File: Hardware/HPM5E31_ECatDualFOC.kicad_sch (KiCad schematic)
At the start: 19 parts, among them J15 HR911205C, U34 M3, U38 M3, U46 M3, U47 M3

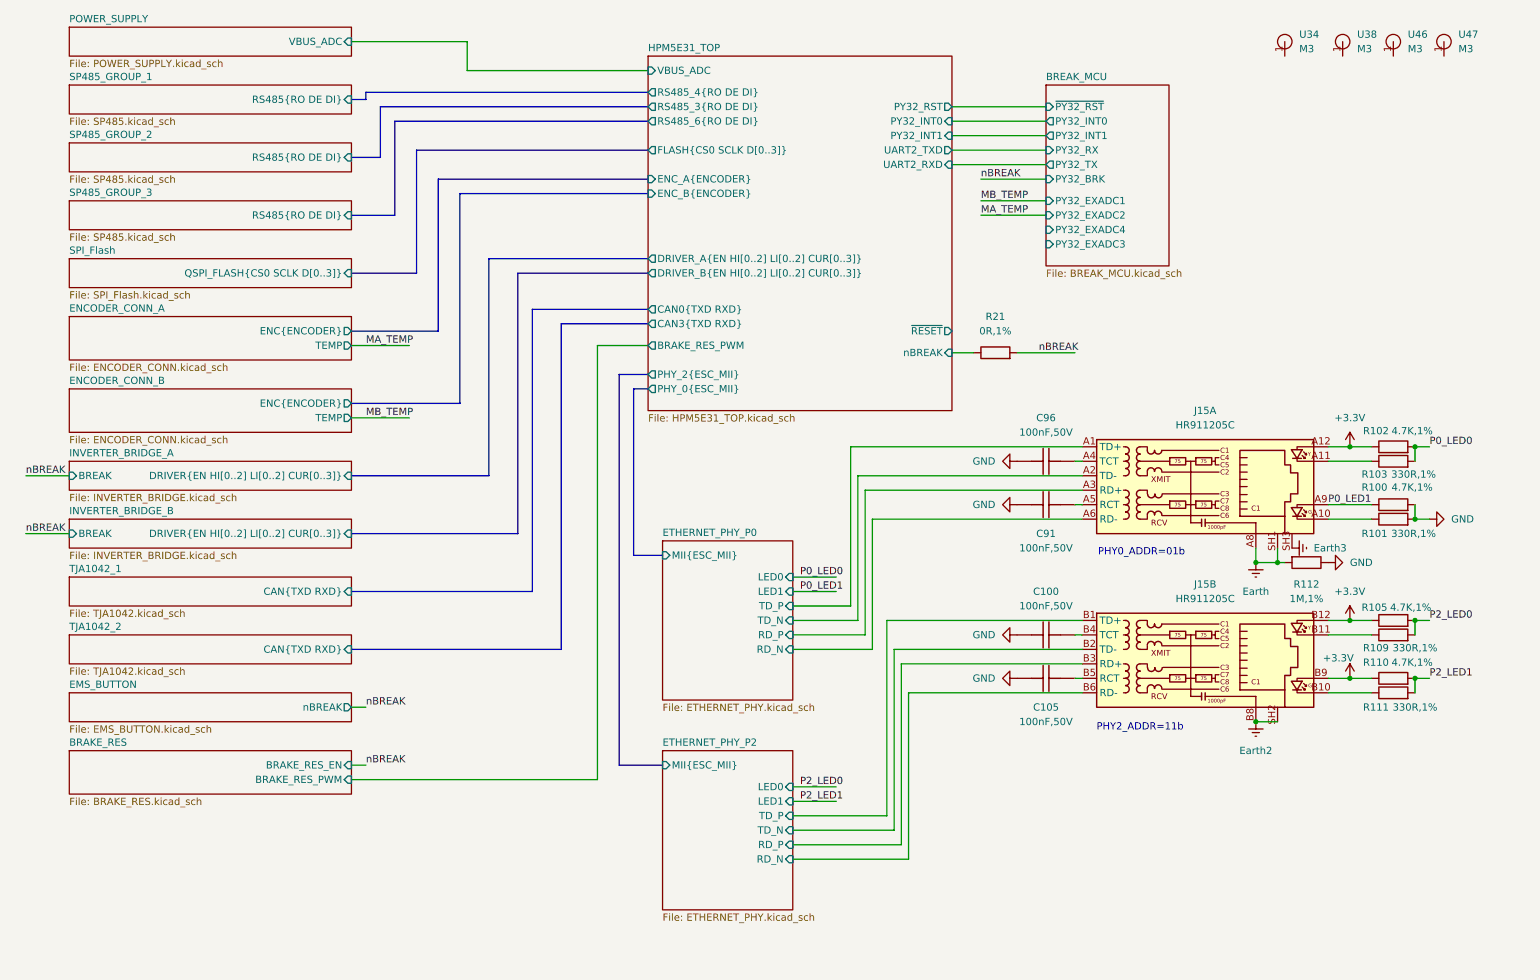
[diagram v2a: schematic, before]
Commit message: PCB：风扇增加控制IO，泄放驱动增加使能引脚，485编码器电源接入控制
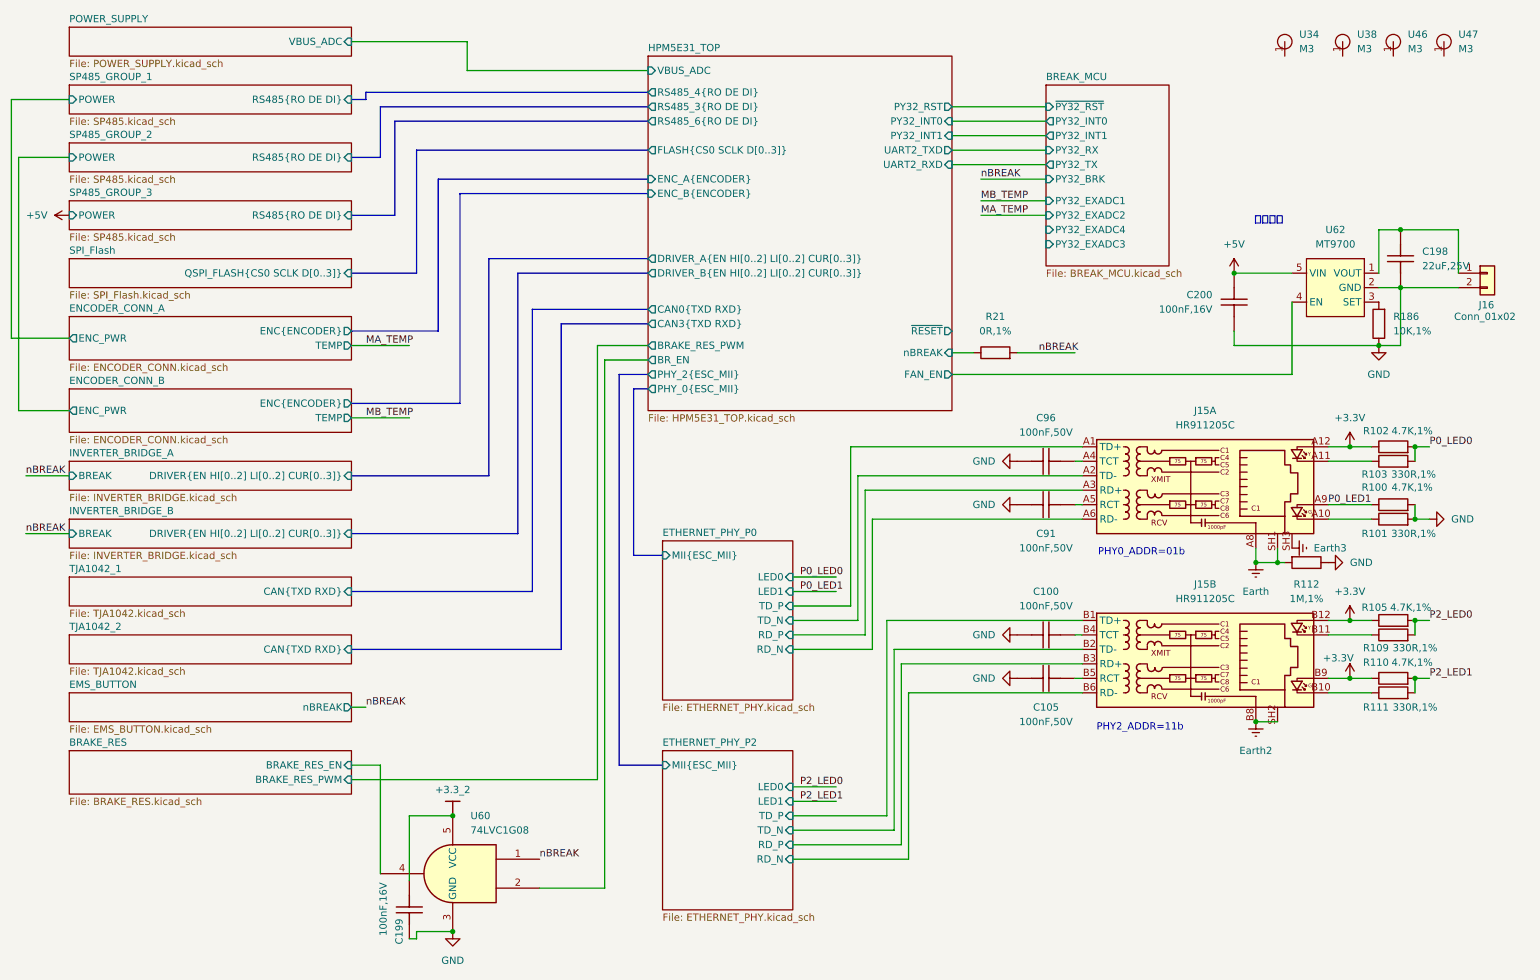
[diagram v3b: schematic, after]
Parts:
- added C198: 22uF,25V, Capacitor_SMD:C_0805_2012Metric, symbol HPM6280Foc:CL21A226MAYNNNE
- added C199, C200: 100nF,16V, Capacitor_SMD:C_0402_1005Metric, symbol HPM6280Foc:CC0402KRX7R7BB104
- added J16: Conn_01x02, Connector_JST:JST_PH_B2B-PH-K_1x02_P2.00mm_Vertical, symbol Connector_Generic:Conn_01x02
- added R186: 10K,1%, Resistor_SMD:R_0402_1005Metric, symbol HPM6280Foc:0402WGF1002TCE
- added U60: 74LVC1G08, Package_TO_SOT_SMD:SOT-353_SC-70-5, symbol 74xGxx:74LVC1G08
- added U62: MT9700, Package_TO_SOT_SMD:SOT-23-5, symbol HPM6280Foc:MT9700
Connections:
- net GND: now also C198.2, C199.2, C200.1, J16.2 (Pin_2), R186.1, U60.3 (GND), U62.2 (GND)
- net nBREAK: now also U60.1
- new net: C198.1, J16.1 (Pin_1), U62.1 (VOUT)
- new net: R186.2, U62.3 (SET)
- new net +3.3_2: C199.1, U60.5 (VCC)
- new net +5V: C200.2, U62.5 (VIN)
- new net BRAKE_RES/BRAKE_RES_EN: U60.4
- new net HPM5E31_TOP/BR_EN: U60.2
- new net HPM5E31_TOP/FAN_EN: U62.4 (EN)
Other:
- sheet ENCODER_CONN_A ports: added ENC_PWR; removed none
- sheet ENCODER_CONN_B ports: added ENC_PWR; removed none
- sheet HPM5E31_TOP ports: added BR_EN, FAN_EN; removed none
- sheet SP485_GROUP_1 ports: added POWER; removed none
- sheet SP485_GROUP_2 ports: added POWER; removed none
- sheet SP485_GROUP_3 ports: added POWER; removed none
- note added: "风扇控制"
